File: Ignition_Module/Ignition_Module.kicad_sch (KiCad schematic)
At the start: 65 parts, among them J1 Conn_01x01_Pin, J10 Conn_01x01_Pin, J11 Conn_01x01_Pin, J12 Conn_01x01_Pin, J13 Conn_01x01_Pin, J14 Conn_01x01_Pin, J15 Conn_01x01_Pin, J16 Conn_01x01_Pin, J2 Conn_01x01_Pin, J3 Conn_01x01_Pin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

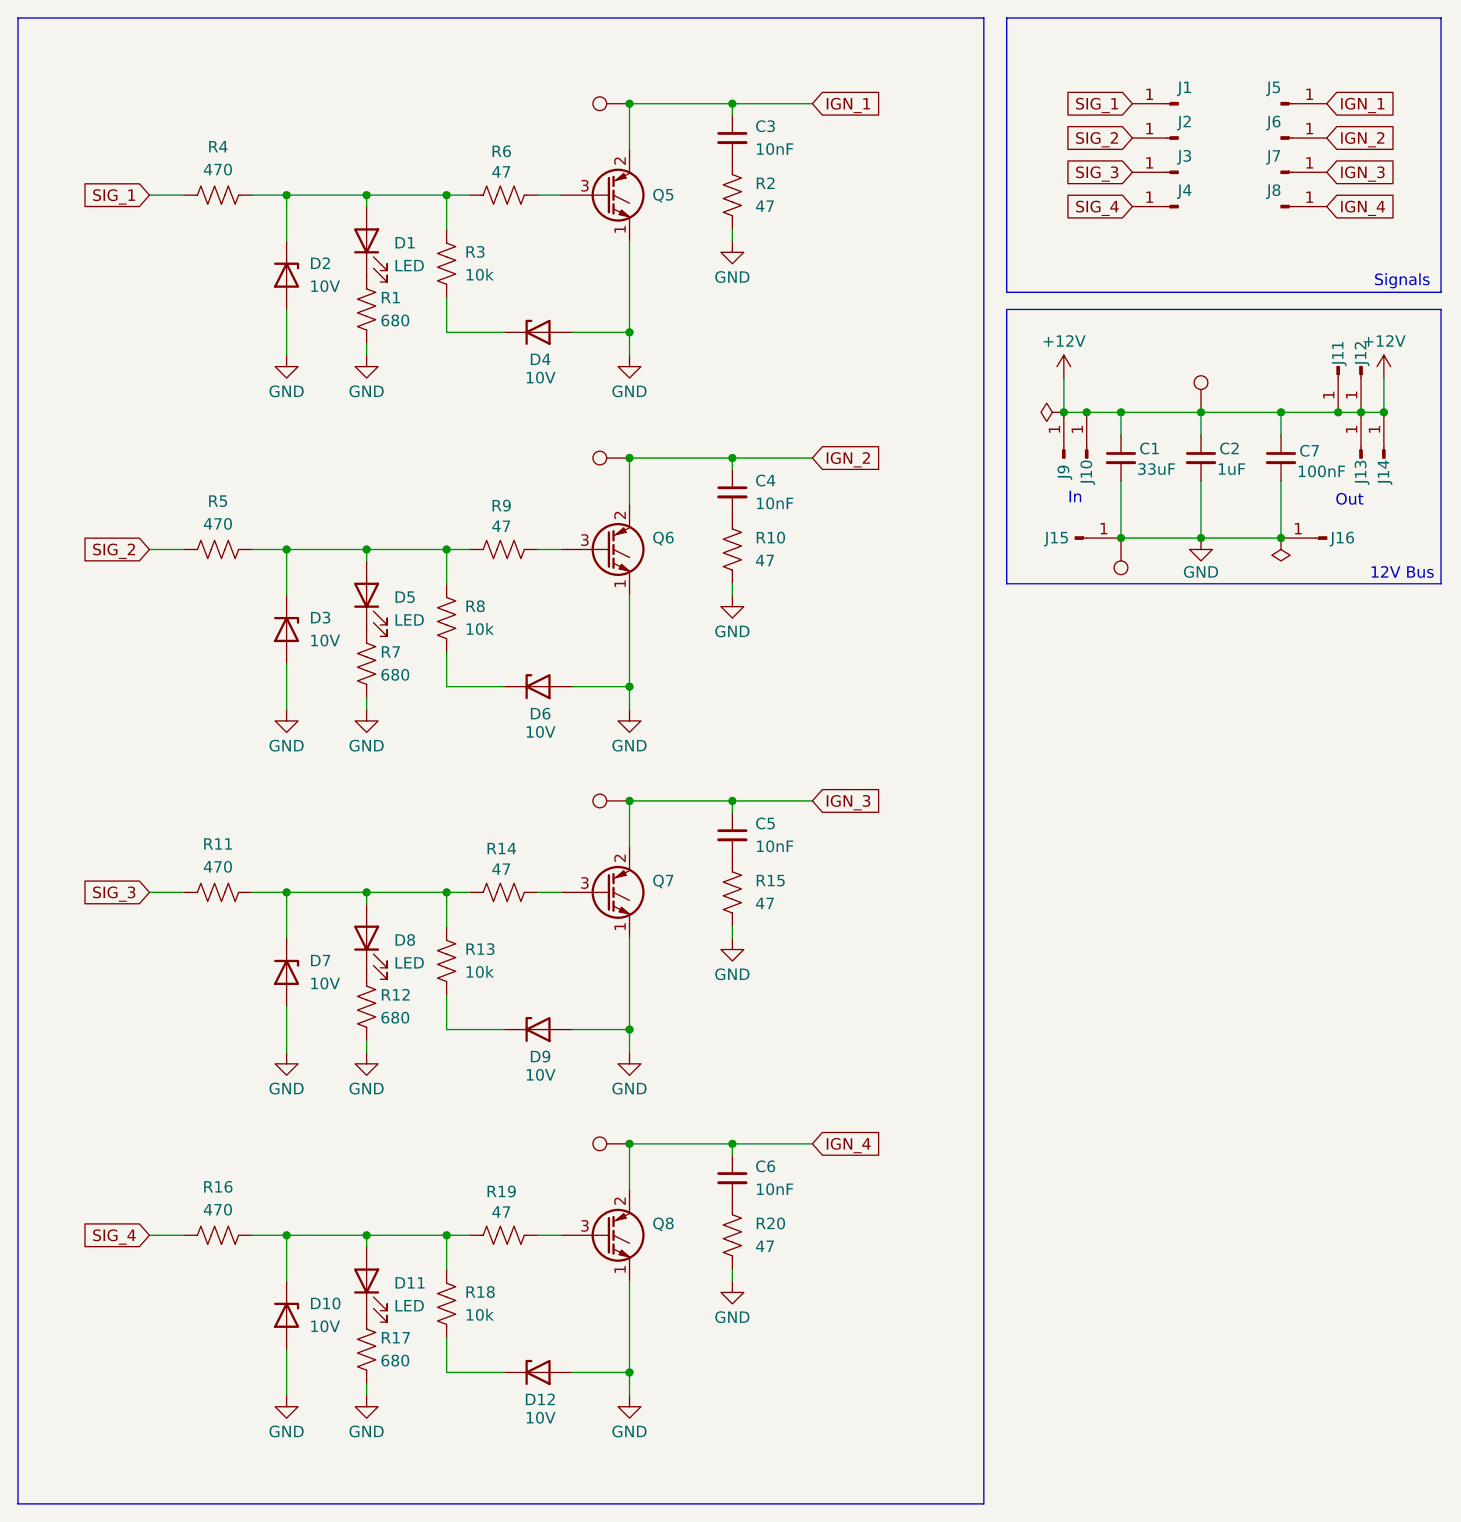
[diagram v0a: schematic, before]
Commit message: removed diode - makes gate float 10V
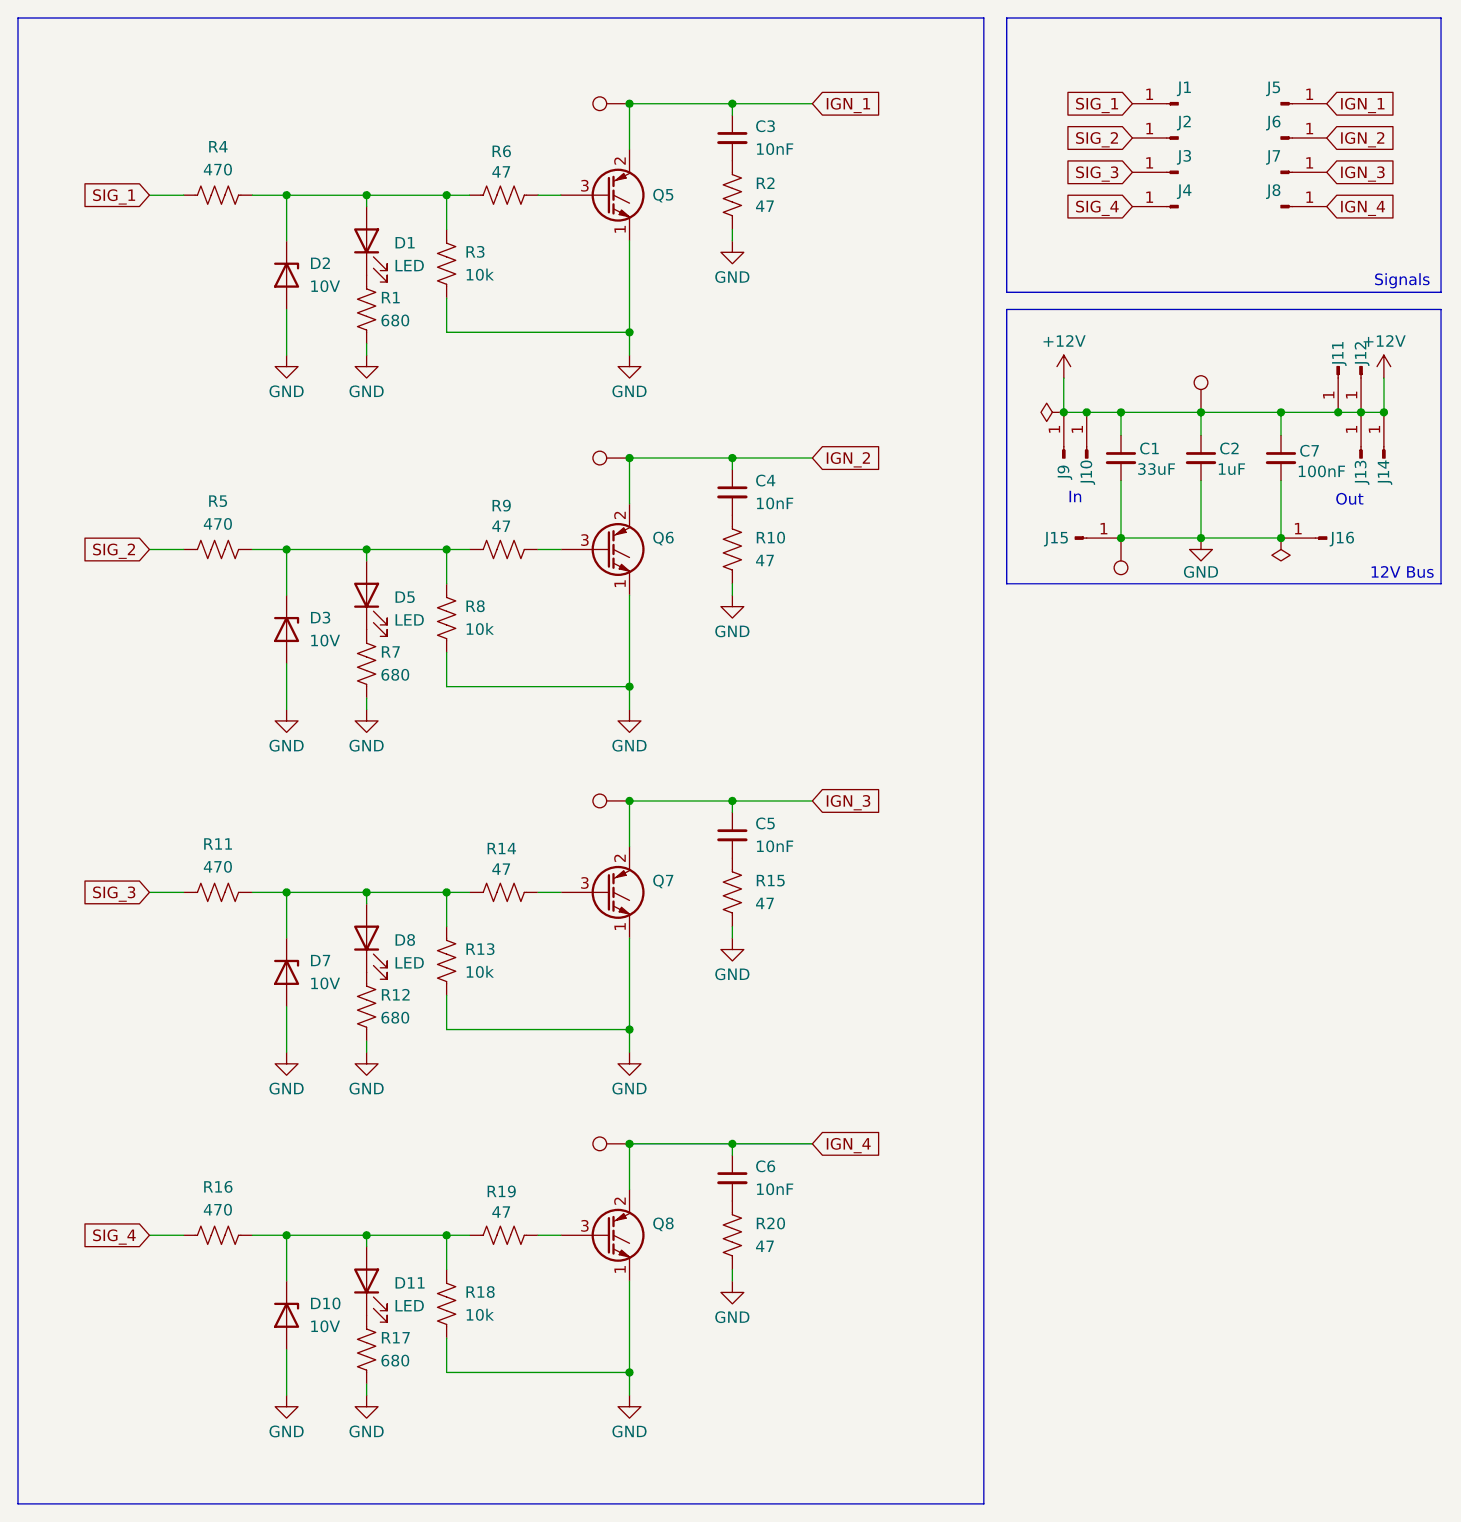
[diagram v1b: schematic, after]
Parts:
- removed D12, D4, D6, D9: 10V, Diode_SMD:D_SOD-523, symbol Device:D_Zener
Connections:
- net GND: now also R13.2, R18.2, R3.2, R8.2
